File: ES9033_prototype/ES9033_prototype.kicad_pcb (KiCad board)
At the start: 4 copper layers, 57.2 x 48.2 mm, 44 parts, among them J101 Conn_01x02, J102 Conn_01x04, J103 Conn_01x04, J104 Conn_01x04, U201 ES9033, U301 LT3042, X201 ECS-2520MV-xxx-xx

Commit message: changed header
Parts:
- removed J102, J103: Conn_01x04, Connector_PinHeader_2.54mm:PinHeader_1x04_P2.54mm_Vertical
- added J1: Conn_02x04_Counter_Clockwise, Connector_PinHeader_2.54mm:PinHeader_2x04_P2.54mm_Vertical, F.Cu at (13.2, 54.0)
- added J2: Conn_02x04_Counter_Clockwise, Connector_PinHeader_2.54mm:PinHeader_2x04_P2.54mm_Vertical, F.Cu at (17.6, 54.0)
- added J3: Conn_02x02_Counter_Clockwise, Connector_PinHeader_2.54mm:PinHeader_2x02_P2.54mm_Vertical, F.Cu at (27.9, 54.0)
- moved NT201 30.0 mm to (16.7, 38.2)
- moved NT202 30.0 mm to (19.2, 38.2)
- moved NT203 30.0 mm to (24.2, 38.2)
- moved NT204 30.0 mm to (21.7, 38.2)
- moved JP205 3.51 mm to (60.5, 59.0)
- moved JP206 1.25 mm to (66.9, 52.5)
- moved R206 1.25 mm to (62.8, 49.5)
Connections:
- U201 pad 26: /DAC_ES9033/DAC_MCLK -> /DAC_ES9033/MCLK_DAC_IN
- X201 pad 3: /DAC_ES9033/DAC_MCLK -> Net-(X201-Pad3)
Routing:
- net /DAC_ES9033/HW2: track 24.9 -> 11.2 mm
- net Net-(X201-Pad3): track 0.00 -> 6.11 mm
- net /DAC_ES9033/DAC_MCLK: track 6.11 -> 0.00 mm
- net Net-(JP204-Pad2): track 5.94 -> 0.00 mm
- net Net-(JP205-Pad3): track 5.84 -> 6.99 mm

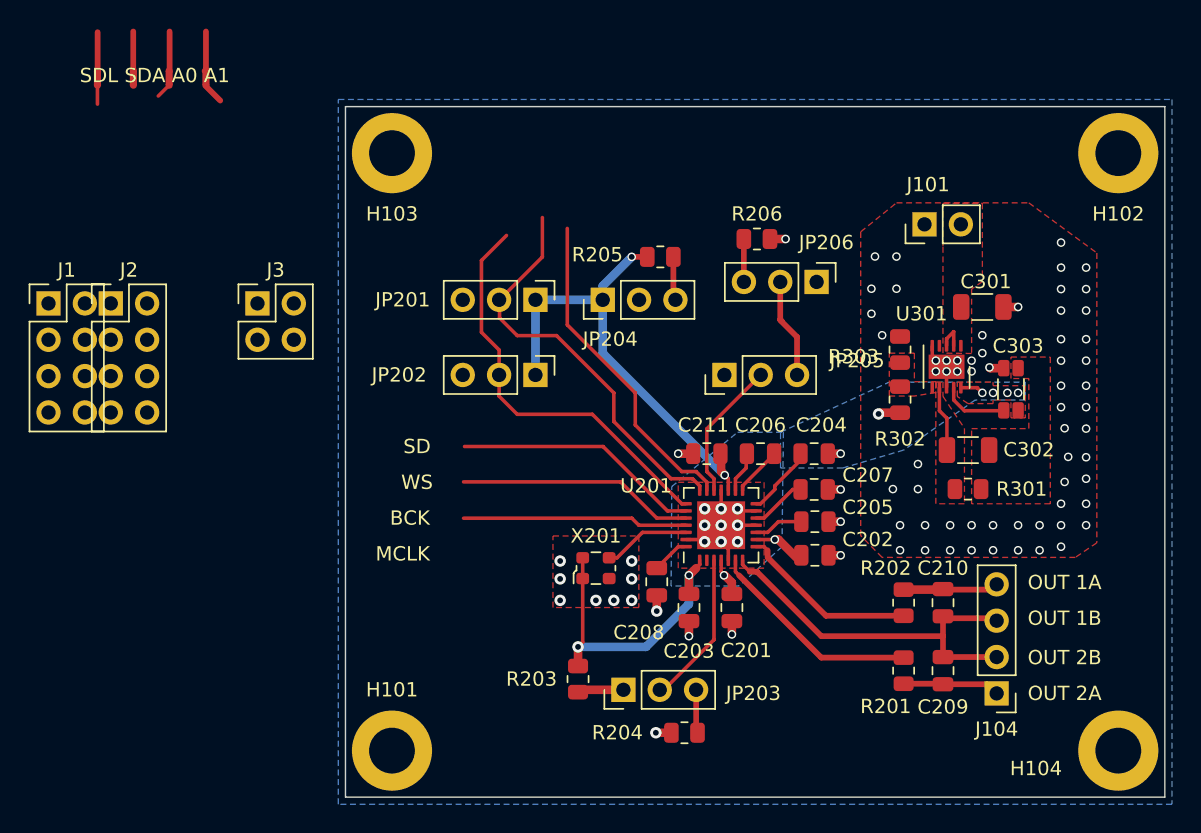
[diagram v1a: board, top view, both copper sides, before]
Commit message: changed header placement
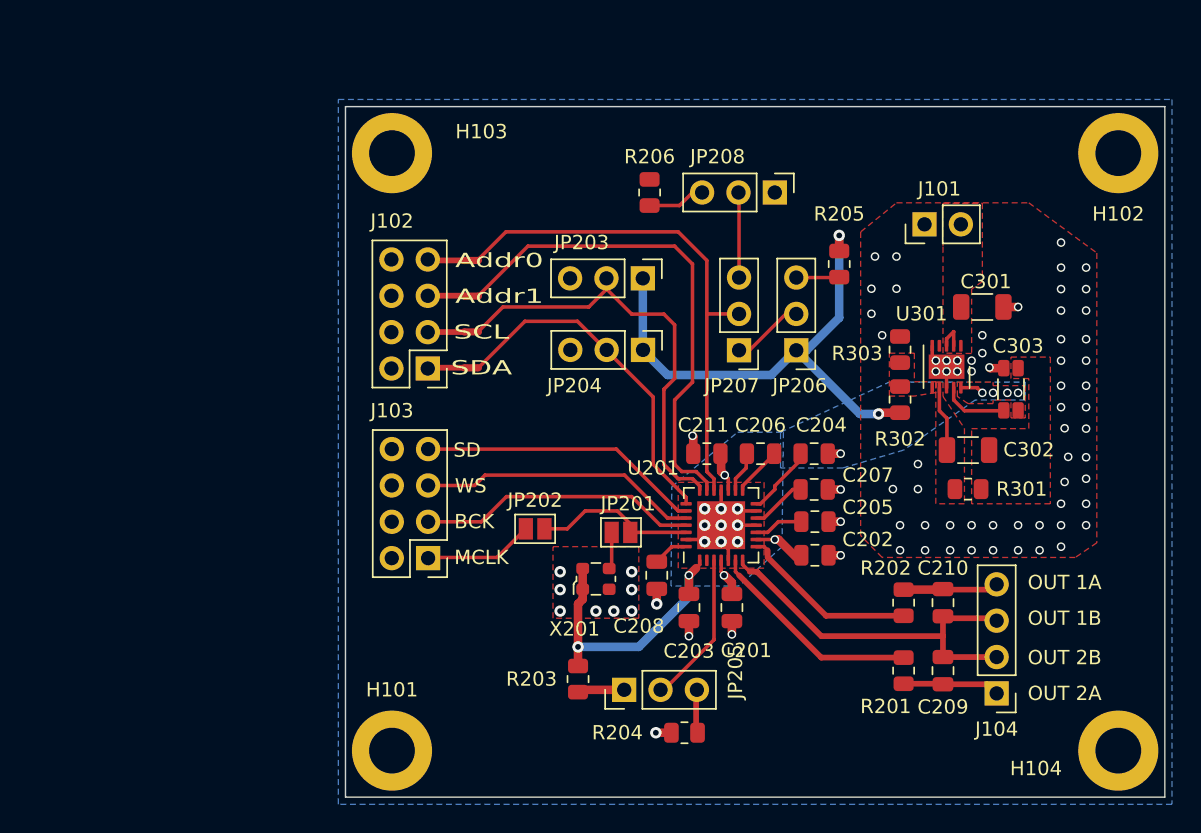
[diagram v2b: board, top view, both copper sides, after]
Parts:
- removed J1, J2: Conn_02x04_Counter_Clockwise, Connector_PinHeader_2.54mm:PinHeader_2x04_P2.54mm_Vertical
- removed J3: Conn_02x02_Counter_Clockwise, Connector_PinHeader_2.54mm:PinHeader_2x02_P2.54mm_Vertical
- added J102: conn_2x4_P2.52mm, Connector_PinHeader_2.54mm:PinHeader_2x04_P2.54mm_Vertical, F.Cu at (39.8, 58.5)
- added J103: conn_2x4_P2.52mm, Connector_PinHeader_2.54mm:PinHeader_2x04_P2.54mm_Vertical, F.Cu at (39.8, 71.8)
- added JP207: Jumper_3_Open, Connector_PinHeader_2.54mm:PinHeader_1x03_P2.54mm_Vertical, F.Cu at (61.5, 57.3)
- added JP208: Jumper_3_Open, Connector_PinHeader_2.54mm:PinHeader_1x03_P2.54mm_Vertical, F.Cu at (64.0, 46.2)
- JP201, JP202: value Jumper_3_Open -> jumper_open; footprint Connector_PinHeader_2.54mm:PinHeader_1x03_P2.54mm_Vertical -> Jumper:SolderJumper-2_P1.3mm_Open_Pad1.0x1.5mm
- moved NT201 33.1 mm to (42.8, 58.5), turned to 0 degrees
- moved NT202 29.5 mm to (42.8, 56.0), turned to 0 degrees
- moved JP203 28.8 mm to (54.8, 52.2), turned to -90 degrees
- moved NT204 26.0 mm to (42.8, 53.5), turned to 0 degrees
- moved JP205 23.1 mm to (53.5, 81.0)
- moved NT203 22.5 mm to (42.8, 51.0), turned to 0 degrees
- moved JP201 17.3 mm to (53.2, 70.0), turned to 0 degrees
- moved R205 12.5 mm to (68.5, 51.2), turned to 90 degrees
- moved JP202 10.8 mm to (47.2, 69.8), turned to 180 degrees
- moved R206 8.17 mm to (55.2, 46.2), turned to 90 degrees
- moved JP206 4.98 mm to (65.5, 57.3), turned to 180 degrees
- moved JP204 4.49 mm to (54.8, 57.2), turned to -90 degrees
- moved X201 0.75 mm to (51.5, 73.2)
- moved C208 0.45 mm to (55.8, 73.0)
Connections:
- JP201 pad 1: +3V3 -> Net-(JP201-Pad1)
- JP201 pad 2: /DAC_ES9033/HW1 -> /DAC_ES9033/MCLK_DAC_IN
- JP202 pad 1: +3V3 -> /DAC_ES9033/MCLK_DAC_IN
- JP202 pad 2: /DAC_ES9033/HW0 -> /DAC_ES9033/MCLK
- JP203 pad 1: Net-(JP203-Pad1) -> +3V3
- JP203 pad 2: /DAC_ES9033/MODE -> /DAC_ES9033/HW1
- JP203 pad 3: Net-(JP203-Pad3) -> GND
- JP204 pad 2: Net-(JP204-Pad2) -> /DAC_ES9033/HW0
- JP204 pad 3: Net-(JP204-Pad3) -> GND
- JP205 pad 1: Net-(JP204-Pad2) -> Net-(JP205-Pad1)
- JP205 pad 2: /DAC_ES9033/HW2 -> /DAC_ES9033/MODE
- JP206 pad 1: GND -> +3V3
- JP206 pad 2: Net-(JP205-Pad3) -> Net-(JP206-Pad2)
- R203 pad 1: Net-(JP203-Pad1) -> Net-(JP205-Pad1)
- R204 pad 1: Net-(JP203-Pad3) -> Net-(JP205-Pad3)
- R205 pad 1: Net-(JP204-Pad3) -> Net-(JP206-Pad3)
- R206 pad 1: Net-(JP206-Pad3) -> Net-(JP208-Pad3)
- X201 pad 3: Net-(X201-Pad3) -> Net-(JP201-Pad1)
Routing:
- net /DAC_ES9033/HW2: track 11.2 -> 36.1 mm
- net /DAC_ES9033/MCLK_DAC_IN: track 0.00 -> 11.4 mm
- net /DAC_ES9033/MUTE_CTRL: track 24.0 -> 34.8 mm
- net /DAC_ES9033/MCLK: track 0.00 -> 7.67 mm
- net Net-(X201-Pad3): track 6.11 -> 0.00 mm
- net Net-(JP207-Pad3): track 0.00 -> 6.07 mm
- net /DAC_ES9033/HW0: track 29.9 -> 24.2 mm
- net Net-(JP206-Pad2): track 0.00 -> 5.30 mm
- net Net-(JP205-Pad3): track 6.99 -> 2.28 mm
- net Net-(JP208-Pad3): track 0.00 -> 4.47 mm
- net /DAC_ES9033/DAC_BCK: track 15.8 -> 19.6 mm
- net +3V3: track 64.1 -> 67.8 mm
- net Net-(JP204-Pad3): track 3.08 -> 0.00 mm
- net Net-(JP205-Pad1): track 0.00 -> 3.06 mm
- net Net-(JP203-Pad1): track 3.06 -> 0.00 mm
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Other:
- board text added: "Addr0"
- board text added: "Addr1"
- board text added: "SCL"
- board text added: "SDA"
- board text removed: "SDL SDA A0 A1"

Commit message: stuff
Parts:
- added SW201: SW_SP3T, Button_Switch_SMD:SW_SP3T_PCM13, F.Cu at (47.0, 85.0)
- added U302: LT3042, Package_DFN_QFN:DFN-10-1EP_3x3mm_P0.5mm_EP1.7x2.5mm, F.Cu at (76.1, 58.4)
- U301: value LT3042 -> TVS1400DRV; footprint Package_DFN_QFN:DFN-10-1EP_3x3mm_P0.5mm_EP1.7x2.5mm -> Package_SON:WSON-6-1EP_2x2mm_P0.65mm_EP1x1.6mm
- moved U301 11.4 mm to (75.1, 47.1), turned to 0 degrees
- moved R204 6.79 mm to (64.0, 81.5), turned to 90 degrees
- moved J101 4.73 mm to (74.6, 43.8)
- moved R203 2.75 mm to (53.0, 80.2)
- moved JP205 2.50 mm to (56.0, 81.0)
- moved C208 0.10 mm to (55.8, 73.1)
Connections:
- U201 pad 2: /DAC_ES9033/DAC_ENABLE -> Net-(U201-Pad2)
- U301 pad 1: +5V -> GND
- U301 pad 2: +5V -> GND
- U301 pad 3: +5V -> GND
- U301 pad 4: unconnected-(U301-Pad4) -> +5V
- U301 pad 5: GND -> +5V
- U301 pad 6: Net-(R302-Pad2) -> +5V
- U301 pad 7: Net-(C302-Pad1) -> GND
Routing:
- net Net-(U201-Pad2): track 0.00 -> 19.9 mm
- net +3V3: track 67.8 -> 73.2 mm, vias 11 -> 12
- net GND: track 45.7 -> 47.6 mm
- net Net-(JP205-Pad1): track 3.06 -> 2.04 mm
- net /DAC_ES9033/MODE: track 10.5 -> 9.56 mm
- net +5V: track 2.18 -> 3.08 mm

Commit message: removed grounding from mounting holes
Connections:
- H101 pad 1: GND -> unconnected-(H101-Pad1)
- H102 pad 1: GND -> unconnected-(H102-Pad1)
- H103 pad 1: GND -> unconnected-(H103-Pad1)
- H104 pad 1: GND -> unconnected-(H104-Pad1)
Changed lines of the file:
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@@
   (net 37 "Net-(JP201-Pad1)")
   (net 38 "unconnected-(U302-Pad4)")
-  (net 39 "Net-(U201-Pad2)")
+  (net 39 "unconnected-(H101-Pad1)")
   (net 40 "/DAC_ES9033/DAC_ENABLE")
+  (net 41 "unconnected-(H102-Pad1)")
+  (net 42 "unconnected-(H103-Pad1)")
+  (net 43 "unconnected-(H104-Pad1)")
+  (net 44 "Net-(SW201-Pad3)")
   (footprint "Jumper:SolderJumper-2_P1.3mm_Open_Pad1.0x1.5mm" (layer "F.Cu")
     (at 47.25 69.75 180)
@@
     (fp_circle (center 0 0) (end 3.05 0) (layer "F.CrtYd") (width 0.05) (fill none))
     (pad "1" thru_hole circle (at 0 0) (size 5.6 5.6) (drill 3.2) (layers *.Cu *.Mask)
-      (net 1 "GND") (pinfunction "1") (pintype "input"))
+      (net 39 "unconnected-(H101-Pad1)") (pinfunction "1") (pintype "input+no_connect"))
   )
   (footprint "Connector_PinHeader_2.54mm:PinHeader_1x03_P2.54mm_Vertical" (layer "F.Cu")
@@
     (fp_circle (center 0 0) (end 3.05 0) (layer "F.CrtYd") (width 0.05) (fill none))
     (pad "1" thru_hole circle (at 0 0) (size 5.6 5.6) (drill 3.2) (layers *.Cu *.Mask)
-      (net 1 "GND") (pinfunction "1") (pintype "input"))
+      (net 42 "unconnected-(H103-Pad1)") (pinfunction "1") (pintype "input+no_connect"))
   )
   (footprint "Connector_PinHeader_2.54mm:PinHeader_1x03_P2.54mm_Vertical" (layer "F.Cu")
@@
     (fp_circle (center 0 0) (end 3.05 0) (layer "F.CrtYd") (width 0.05) (fill none))
     (pad "1" thru_hole circle (at 0 0) (size 5.6 5.6) (drill 3.2) (layers *.Cu *.Mask)
-      (net 1 "GND") (pinfunction "1") (pintype "input"))
+      (net 41 "unconnected-(H102-Pad1)") (pinfunction "1") (pintype "input+no_connect"))
   )
   (footprint "Connector_PinHeader_2.54mm:PinHeader_1x03_P2.54mm_Vertical" (layer "F.Cu")
@@
     (fp_circle (center 0 0) (end 3.05 0) (layer "F.CrtYd") (width 0.05) (fill none))
     (pad "1" thru_hole circle (at 0 0) (size 5.6 5.6) (drill 3.2) (layers *.Cu *.Mask)
-      (net 1 "GND") (pinfunction "1") (pintype "input"))
+      (net 43 "unconnected-(H104-Pad1)") (pinfunction "1") (pintype "input+no_connect"))
   )
   (footprint "Resistor_SMD:R_0805_2012Metric" (layer "F.Cu")
@@
       (net 40 "/DAC_ES9033/DAC_ENABLE") (pinfunction "2") (pintype "passive"))
     (pad "3" smd rect (at 1.5 -1.43) (size 0.7 1.5) (layers "F.Cu" "F.Paste" "F.Mask")
-      (net 39 "Net-(U201-Pad2)") (pinfunction "3") (pintype "passive"))
+      (net 44 "Net-(SW201-Pad3)") (pinfunction "3") (pintype "passive"))
     (pad "4" smd rect (at 3 -1.43) (size 0.7 1.5) (layers "F.Cu" "F.Paste" "F.Mask")
       (net 29 "+3V3") (pinfunction "4") (pintype "passive"))
@@
       (net 29 "+3V3") (pinfunction "AVDD") (pintype "power_in"))
     (pad "2" smd roundrect (at -2.45 -1 90) (size 0.8 0.25) (layers "F.Cu" "F.Paste" "F.Mask") (roundrect_rratio 0.25)
-      (net 39 "Net-(U201-Pad2)") (pinfunction "CHIP_EN") (pintype "bidirectional"))
+      (net 44 "Net-(SW201-Pad3)") (pinfunction "CHIP_EN") (pintype "bidirectional"))
     (pad "3" smd roundrect (at -2.45 -0.5 90) (size 0.8 0.25) (layers "F.Cu" "F.Paste" "F.Mask") (roundrect_rratio 0.25)
       (net 23 "/DAC_ES9033/MODE") (pinfunction "MODE") (pintype "bidirectional"))
@@
   (segment (start 52.6 72.35) (end 52.425 72.525) (width 0.25) (layer "F.Cu") (net 37))
   (segment (start 52.6 70) (end 52.6 72.35) (width 0.25) (layer "F.Cu") (net 37))
-  (segment (start 55.25 79.25) (end 54.25 80.25) (width 0.25) (layer "F.Cu") (net 39))
-  (segment (start 59.25 77.25) (end 57.25 79.25) (width 0.25) (layer "F.Cu") (net 39))
-  (segment (start 54.25 80.25) (end 50.5 80.25) (width 0.25) (layer "F.Cu") (net 39))
-  (segment (start 59.25 71.95) (end 59.25 77.25) (width 0.25) (layer "F.Cu") (net 39))
-  (segment (start 57.25 79.25) (end 55.25 79.25) (width 0.25) (layer "F.Cu") (net 39))
-  (segment (start 50.5 80.25) (end 48.5 82.25) (width 0.25) (layer "F.Cu") (net 39))
-  (segment (start 48.5 82.25) (end 48.5 84.07) (width 0.25) (layer "F.Cu") (net 39))
+  (segment (start 55.25 79.25) (end 54.25 80.25) (width 0.25) (layer "F.Cu") (net 44))
+  (segment (start 59.25 77.25) (end 57.25 79.25) (width 0.25) (layer "F.Cu") (net 44))
+  (segment (start 54.25 80.25) (end 50.5 80.25) (width 0.25) (layer "F.Cu") (net 44))
+  (segment (start 59.25 71.95) (end 59.25 77.25) (width 0.25) (layer "F.Cu") (net 44))
+  (segment (start 57.25 79.25) (end 55.25 79.25) (width 0.25) (layer "F.Cu") (net 44))
+  (segment (start 50.5 80.25) (end 48.5 82.25) (width 0.25) (layer "F.Cu") (net 44))
+  (segment (start 48.5 82.25) (end 48.5 84.07) (width 0.25) (layer "F.Cu") (net 44))
   (zone (net 1) (net_name "GND") (layer "F.Cu") (hatch edge 0.508)
     (connect_pads yes (clearance 0.254))
